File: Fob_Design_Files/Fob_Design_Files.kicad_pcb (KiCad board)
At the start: 2 copper layers, 48.8 x 76.8 mm, 27 parts, among them IC2 TLV70030DDCT, U1 MAX16054AZT_T, U2 CC1101RGPR, U3 BU2032SM-JJ-GTR, U4 STM32C011F4Px, Y1 NX3225GA-26.000MHZ-EXS00A-CG0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

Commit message: Completed schematic
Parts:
- added J1: Conn_01x04_Pin, Connector_PinHeader_2.54mm:PinHeader_1x04_P2.54mm_Vertical, F.Cu at (192.3, 81.8)

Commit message: Updated readme:
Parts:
- moved J1 2.03 mm to (190.2, 81.8)
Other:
- board size 48.8 x 76.8 mm -> 45.6 x 76.8 mm
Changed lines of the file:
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@@
 		(at 170.705 85.019 180)
 		(property "Reference" "U1"
-			(at -0.068 -2.2064 360)
+			(at -0.068 -2.2064 0)
 			(layer "F.SilkS")
 			(effects
@@
 		)
 		(property "Value" "MAX16054AZT_T"
-			(at 4.4024 2.1936 360)
+			(at 4.4024 2.1936 0)
 			(layer "F.Fab")
 			(effects
@@
 		)
 		(property "Footprint" "MAX16054AZT_T:SOT95P275X110-6N"
-			(at 0 0 360)
+			(at 0 0 0)
 			(layer "F.Fab")
 			(hide yes)
@@
 		)
 		(property "Datasheet" ""
-			(at 0 0 360)
+			(at 0 0 0)
 			(layer "F.Fab")
 			(hide yes)
@@
 		)
 		(property "Description" ""
-			(at 0 0 360)
+			(at 0 0 0)
 			(layer "F.Fab")
 			(hide yes)
@@
 		(tags "capacitor")
 		(property "Reference" "C5"
-			(at 0 -1.43 360)
+			(at 0 -1.43 0)
 			(layer "F.SilkS")
 			(effects
@@
 		)
 		(property "Value" "0.1uF"
-			(at 0 1.43 360)
+			(at 0 1.43 0)
 			(layer "F.Fab")
 			(effects
@@
 		)
 		(fp_text user "${REFERENCE}"
-			(at 0 0 360)
+			(at 0 0 0)
 			(layer "F.Fab")
 			(effects
@@
 		(tags "Integrated Circuit")
 		(property "Reference" "IC2"
-			(at 0.107 2.86 360)
+			(at 0.107 2.86 0)
 			(layer "F.SilkS")
 			(effects
@@
 		)
 		(property "Value" "TLV70030DDCT"
-			(at 0 0 360)
+			(at 0 0 0)
 			(layer "F.SilkS")
 			(hide yes)
@@
 		)
 		(property "Footprint" "SamacSys_Parts:SOT95P280X110-5N"
-			(at 0 0 360)
+			(at 0 0 0)
 			(layer "F.Fab")
 			(hide yes)
@@
 		)
 		(property "Datasheet" "http://www.ti.com/lit/gpn/tlv700"
-			(at 0 0 360)
+			(at 0 0 0)
 			(layer "F.Fab")
 			(hide yes)
@@
 		)
 		(property "Description" "Texas Instruments TLV70030DDCT, Low Noise LDO Voltage Regulator, 200mA, 3 V 2%, 2  5.5 Vin, 5-Pin SOT"
-			(at 0 0 360)
+			(at 0 0 0)
 			(layer "F.Fab")
 			(hide yes)
@@
 		)
 		(fp_text user "${REFERENCE}"
-			(at 0 0 360)
+			(at 0 0 0)
 			(layer "F.Fab")
 			(effects
@@
 	(footprint "Connector_PinHeader_2.54mm:PinHeader_1x04_P2.54mm_Vertical"
 		(layer "F.Cu")
-		(at 192.278 81.788)
+		(at 190.246 81.788)
 		(descr "Through hole straight pin header, 1x04, 2.54mm pitch, single row")
 		(tags "Through hole pin header THT 1x04 2.54mm single row")
@@
 	)
 	(gr_rect
-		(start 146.177 42.164)
-		(end 194.945 118.999)
+		(start 147.447 42.164)
+		(end 193.04 118.999)
 		(stroke
 			(width 0.05)
@@
 		(layer "Edge.Cuts")
 	)
+	(dimension
+		(type aligned)
+		(layer "Edge.Cuts")
+		(pts
+			(xy 147.447 42.164) (xy 193.04 42.164)
+		)
+		(height -5.842)
+		(gr_text "45.5930 mm"
+			(at 170.2435 35.172 0)
+			(layer "Edge.Cuts")
+			(effects
+				(font
+					(size 1 1)
+					(thickness 0.15)
+				)
+			)
+		)
+		(format
+			(prefix "")
+			(suffix "")
+			(units 3)
+			(units_format 1)
+			(precision 4)
+		)
+		(style
+			(thickness 0.05)
+			(arrow_length 1.27)
+			(text_position_mode 0)
+			(extension_height 0.58642)
+			(extension_offset 0.5) keep_text_aligned)
+	)
+	(dimension
+		(type aligned)
+		(layer "Edge.Cuts")
+		(pts
+			(xy 147.447 118.999) (xy 147.447 42.164)
+		)
+		(height -7.112)
+		(gr_text "76.8350 mm"
+			(at 139.185 80.5815 90)
+			(layer "Edge.Cuts")
+			(effects
+				(font
+					(size 1 1)
+					(thickness 0.15)
+				)
+			)
+		)
+		(format
+			(prefix "")
+			(suffix "")
+			(units 3)
+			(units_format 1)
+			(precision 4)
+		)
+		(style
+			(thickness 0.05)
+			(arrow_length 1.27)
+			(text_position_mode 0)
+			(extension_height 0.58642)
+			(extension_offset 0.5) keep_text_aligned)
+	)
 )

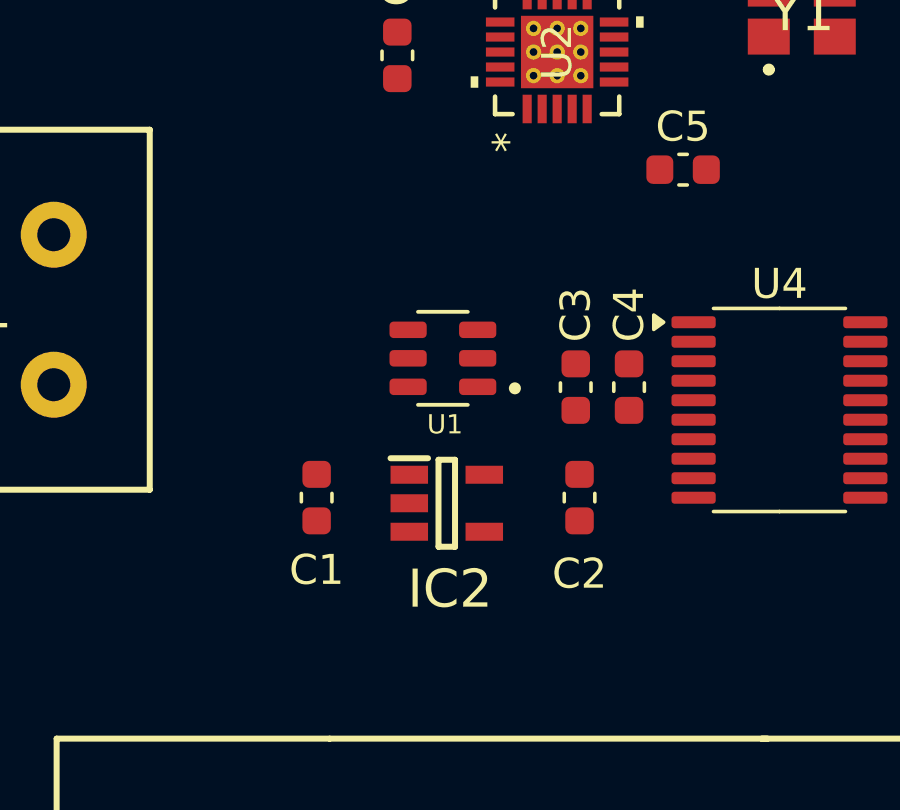
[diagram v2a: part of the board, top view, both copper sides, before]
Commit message: Minor fob schematic changes
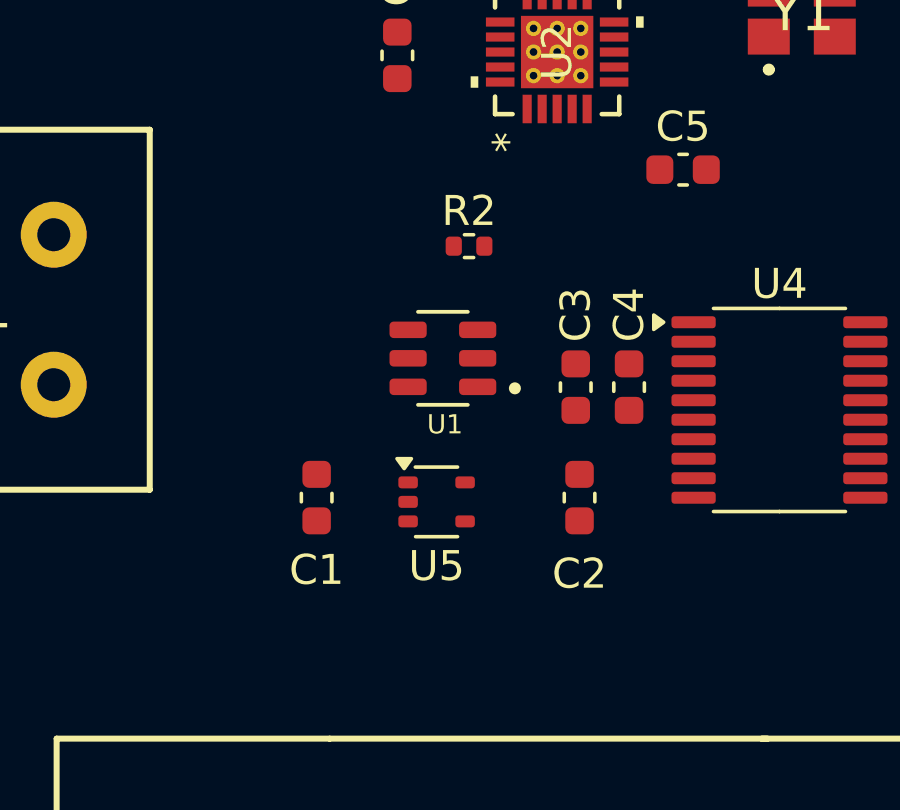
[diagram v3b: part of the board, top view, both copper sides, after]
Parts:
- removed IC2: TLV70030DDCT, SamacSys_Parts:SOT95P280X110-5N
- added R2: 10k, Resistor_SMD:R_0402_1005Metric, F.Cu at (171.6, 81.3)
- added U5: TLV70028_SOT353, Package_TO_SOT_SMD:SOT-353_SC-70-5, F.Cu at (170.5, 89.8)

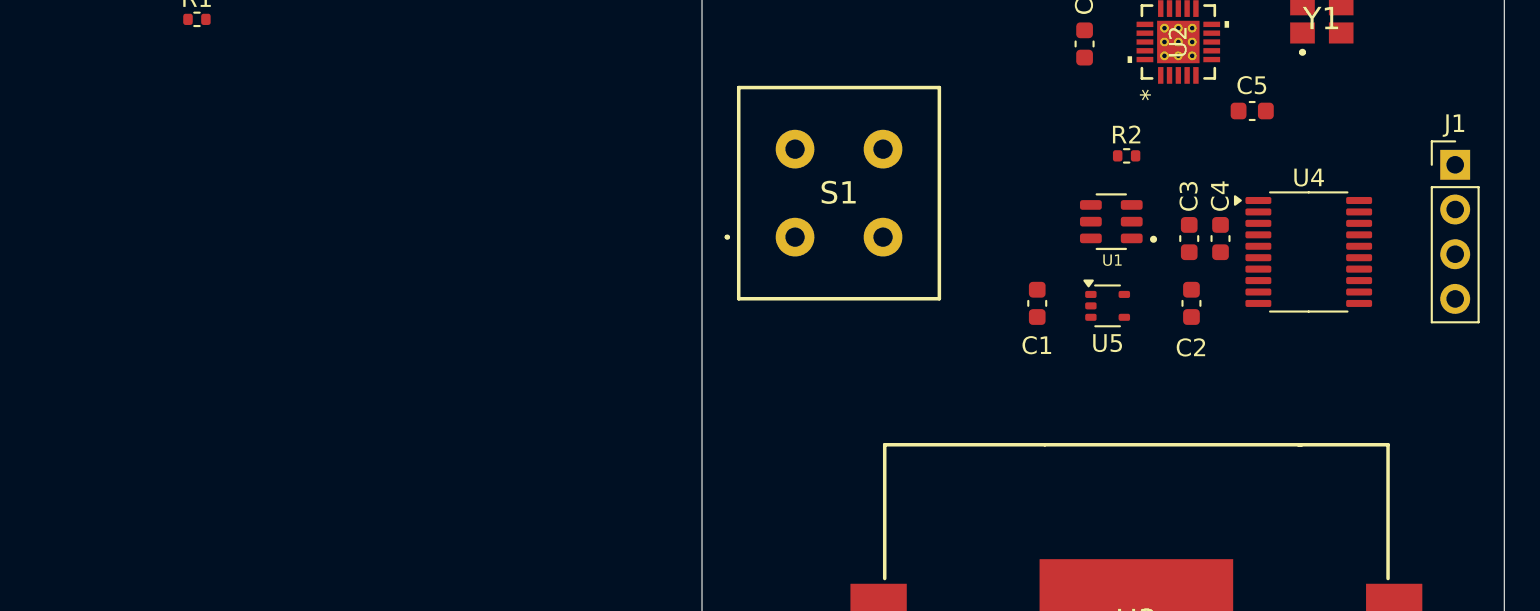
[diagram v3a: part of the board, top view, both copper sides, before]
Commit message: Tolerance anaylsis LaTeX
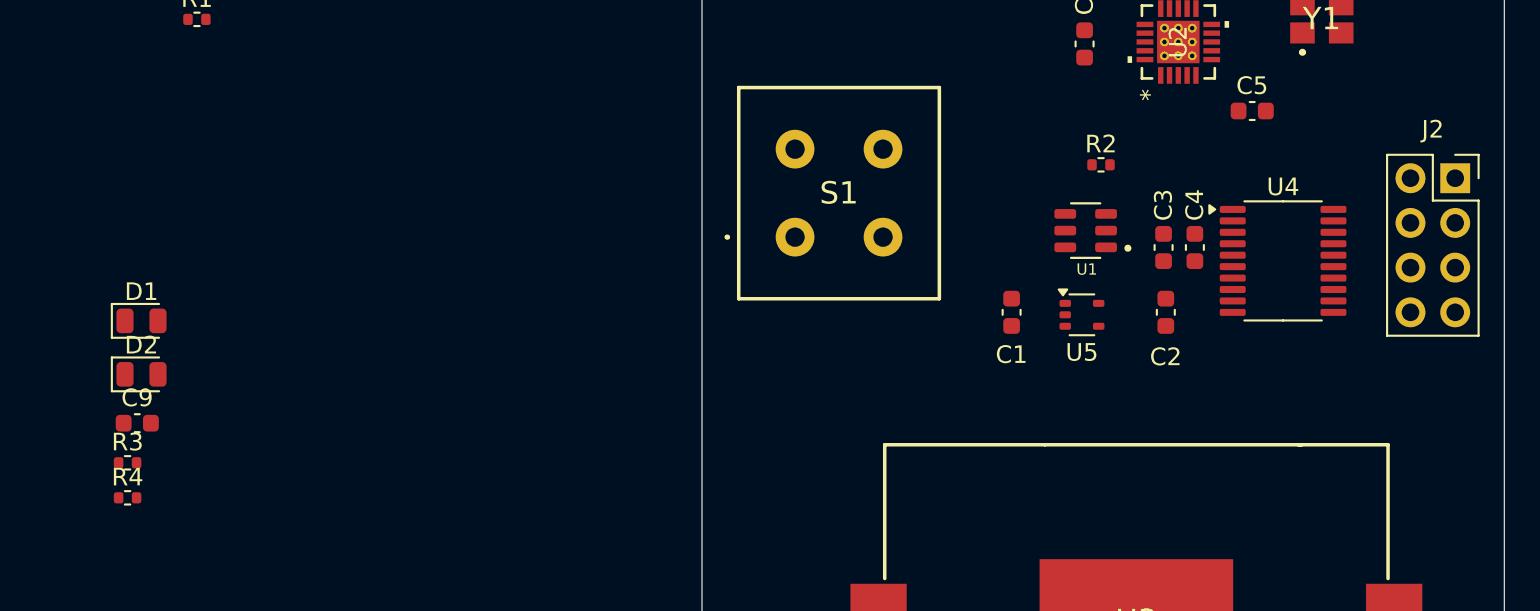
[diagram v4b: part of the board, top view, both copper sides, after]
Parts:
- removed J1: Conn_01x04_Pin, Connector_PinHeader_2.54mm:PinHeader_1x04_P2.54mm_Vertical
- added C9: 0.1uF, Capacitor_SMD:C_0603_1608Metric, F.Cu at (115.4, 96.5)
- added D1: LED, LED_SMD:LED_0805_2012Metric, F.Cu at (115.6, 90.7)
- added D2: LED, LED_SMD:LED_0805_2012Metric, F.Cu at (115.6, 93.7)
- added J2: Conn_02x04_Counter_Clockwise, Connector_PinSocket_2.54mm:PinSocket_2x04_P2.54mm_Vertical, F.Cu at (190.2, 82.5)
- added R3: 330, Resistor_SMD:R_0402_1005Metric, F.Cu at (114.8, 98.7)
- added R4: 330, Resistor_SMD:R_0402_1005Metric, F.Cu at (114.8, 100.7)
- moved C1 1.54 mm to (165.0, 90.2)
- moved C3 1.54 mm to (173.7, 86.5)
- moved C4 1.54 mm to (175.5, 86.5)
- moved R2 1.54 mm to (170.1, 81.8)
- moved U1 1.54 mm to (169.2, 85.5)
- moved U5 1.54 mm to (169.0, 90.3)
- moved C2 1.54 mm to (173.8, 90.2)
- moved U4 1.54 mm to (180.5, 87.2)
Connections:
- net 3V_Button renamed Button
- C1 pad 1: +3V0 -> VBAT
- S1 pad 1: +3V0 -> GND
- S1 pad 2: +3V0 -> GND
- U1 pad 6: +3V0 -> VBAT
- U3 pad 1: +3V0 -> VBAT
- U4 pad 10: unconnected-(U4-PA3-Pad10) -> USART_RX
- U4 pad 14: unconnected-(U4-PA7-Pad14) -> RF_RX_LED
- U4 pad 15: unconnected-(U4-PA8-Pad15) -> USART_TX
- U4 pad 16: unconnected-(U4-PA9/PA11-Pad16) -> RF_TX_LED
- U5 pad 1: +3V0 -> VBAT

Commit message: Done with fob layout
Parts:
- removed D1, D2: LED, LED_SMD:LED_0805_2012Metric
- removed R3, R4: 330, Resistor_SMD:R_0402_1005Metric
- C10, C11, C12, C13, C14, C15, C6, C7: footprint Capacitor_SMD:C_0402_1005Metric -> Capacitor_SMD:C_0603_1608Metric
- J2: value Conn_02x04_Counter_Clockwise -> Conn_02x04_Odd_Even
- L1, L2, L3, L4: footprint Inductor_SMD:L_0402_1005Metric -> Inductor_SMD:L_0603_1608Metric
- R1, R2: footprint Resistor_SMD:R_0402_1005Metric -> Inductor_SMD:L_0603_1608Metric
- moved J2 95.3 mm to (95.0, 80.0)
- moved U4 85.5 mm to (96.0, 74.4), turned to 180 degrees
- moved C5 79.7 mm to (99.5, 70.1)
- moved Y1 79.7 mm to (103.3, 66.9)
- moved U2 79.6 mm to (95.2, 67.2)
- moved C8 78.0 mm to (91.4, 68.2)
- moved C4 75.6 mm to (100.9, 74.4), turned to 90 degrees
- moved C3 72.3 mm to (102.4, 74.4), turned to 90 degrees
- moved R2 68.5 mm to (101.8, 76.8), turned to 180 degrees
- moved C2 67.5 mm to (109.3, 70.2), turned to 0 degrees
- moved U1 62.9 mm to (107.0, 76.8), turned to 0 degrees
- moved U5 62.2 mm to (109.3, 73.0), turned to 90 degrees
- moved C1 60.6 mm to (106.9, 72.9), turned to 90 degrees
- moved E1 60.2 mm to (111.8, 43.1)
- moved U3 59.9 mm to (121.9, 75.0), turned to 90 degrees
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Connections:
- J2 pad 2: SWDIO -> VDD
- J2 pad 3: SWCLK -> SWDIO
- J2 pad 4: GND -> USART_RX
- J2 pad 5: GND -> SWCLK
- J2 pad 7: USART_RX -> GND
- J2 pad 8: VDD -> GND
- U4 pad 14: RF_RX_LED -> unconnected-(U4-PA7-Pad14)
- U4 pad 16: RF_TX_LED -> unconnected-(U4-PA9/PA11-Pad16)
- U4 pad 17: GDO0 -> GDO2
- U4 pad 20: GDO2 -> GDO0
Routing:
- net VBAT: track 0.00 -> 25.5 mm
- net GDO0: track 0.00 -> 22.2 mm, vias 0 -> 2
- net GND: track 0.00 -> 19.4 mm, vias 0 -> 30
- net USART_RX: track 0.00 -> 16.1 mm, vias 0 -> 1
- net Button: track 0.00 -> 14.8 mm, vias 0 -> 1
- net VDD: track 0.00 -> 14.1 mm, vias 0 -> 7
- net SPI_NSS: track 0.00 -> 13.7 mm, vias 0 -> 2
- net USART_TX: track 0.00 -> 13.3 mm
- net SWCLK: track 0.00 -> 11.8 mm
- net SPI_MOSI: track 0.00 -> 11.8 mm, vias 0 -> 2
- net SWDIO: track 0.00 -> 11.2 mm
- net OSC_OUT: track 0.00 -> 10.8 mm
- net SPI_SCLK: track 0.00 -> 10.7 mm, vias 0 -> 2
- net OSC_IN: track 0.00 -> 7.89 mm
- net PWR_DWN: track 0.00 -> 7.66 mm
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- added copper zone on In1.Cu, net GND
- added copper zone on In2.Cu, net VDD
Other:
- board size 45.6 x 76.8 mm -> 42.9 x 62.1 mm
- copper layers 2 -> 4
- board text added: "GND"
- board text added: "RX"
- board text added: "SWCLK"
- board text added: "SWDIO"
- board text added: "Schnorr Protocol Fob V1 Michael Gamota 10-8-2024 ECE 445"
- board text added: "TX"
- board text added: "VDD"

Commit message: Minor changes
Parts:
- removed J2: Conn_02x04_Odd_Even, Connector_PinSocket_2.54mm:PinSocket_2x04_P2.54mm_Vertical
- added J1: Conn_02x03_Odd_Even, Connector_PinSocket_2.54mm:PinSocket_2x03_P2.54mm_Vertical, F.Cu at (95.0, 79.9)
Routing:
- net VDD: track 14.1 -> 16.1 mm
- net GND: track 19.4 -> 19.9 mm

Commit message: New gerbers
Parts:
- moved J1 2.22 mm to (94.7, 82.1)
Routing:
- net GND: track 19.9 -> 63.5 mm, vias 30 -> 53
- net VDD: track 16.1 -> 30.8 mm, vias 7 -> 4
- net SWCLK: track 11.8 -> 14.7 mm
- net USART_TX: track 13.3 -> 15.8 mm
- net USART_RX: track 16.1 -> 18.2 mm, vias 1 -> 2
- net SWDIO: track 11.2 -> 11.8 mm, vias 0 -> 1
- added copper zone on B.Cu, net GND
- added copper zone on F.Cu, net VDD
- removed copper zone on In1.Cu, net GND
- removed copper zone on In2.Cu, net VDD
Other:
- board size 42.9 x 62.1 mm -> 44.7 x 63.5 mm
- copper layers 4 -> 2
